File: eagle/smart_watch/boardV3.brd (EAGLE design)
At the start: 100 x 80 mm, 62 parts, among them U1 MCP73831, U2 TPS61200, U3 MAX1704X, U4 V_REG_LDOSMD, Y1 16MHz

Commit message: Did a little of bit of tweeks on the wireing
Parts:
- removed JP1: USB_MICROB_PLUG-PTH, SparkFun-Connectors:MICRO-B-RA-TH
- added RECHARGE: (no value), SparkFun-Connectors:MOLEX-1X2
- I2C: device SparkFun-Connectors:1X02_PP_HOLES_ONLY -> SparkFun-Connectors:MOLEX-1X2
- JP4: device SparkFun-Connectors:MOLEX-1X4 -> SparkFun-Connectors:1X05
- R12, R13: device SparkFun-Passives:0402-RES -> SparkFun-Resistors:0603-RES
- moved JP4 2.54 mm to (29.7, 1.35)
- moved R12 1.57 mm to (25.7, 15.1), turned to 90 degrees
- moved R18 0.54 mm to (39.2, 5.46)
- moved R13 0.51 mm to (22.4, 14.3)
- moved R17 0.40 mm to (43.1, 7.13)
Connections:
- net 3.3V: now also JP4.5
- net GND: now also RECHARGE.2; no longer JP1.5
- net VBUS: now also RECHARGE.1; no longer JP1.1
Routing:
- net 3.3V: track 108.8 -> 138.9 mm
- net JTAG_RESETX: track 18.7 -> 27.2 mm, vias 1 -> 2
- net SDA: track 45.9 -> 39.3 mm
- net GND: track 109.7 -> 105.5 mm
- net JTAG_TDO_SWOX: track 12.4 -> 15.6 mm, vias 0 -> 1
- net JTAG_TCLK_SWCLKX: track 9.00 -> 12.0 mm, vias 0 -> 1
- net MISO1: track 58.0 -> 60.2 mm, vias 3 -> 1
- net JTAG_TMS_SWDIOX: track 15.5 -> 13.7 mm
- net SSEL1: track 40.1 -> 38.6 mm
- net SCL: track 41.7 -> 40.9 mm
- net N$18: track 2.13 -> 2.67 mm
- net VBUS: track 6.75 -> 6.23 mm

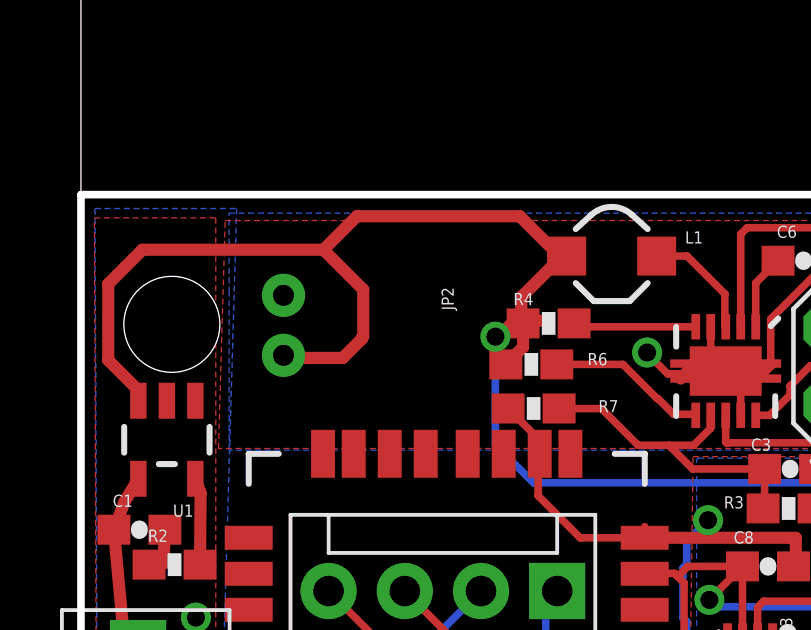
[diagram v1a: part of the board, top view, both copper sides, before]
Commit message: Fixed up git ignore for xpress;
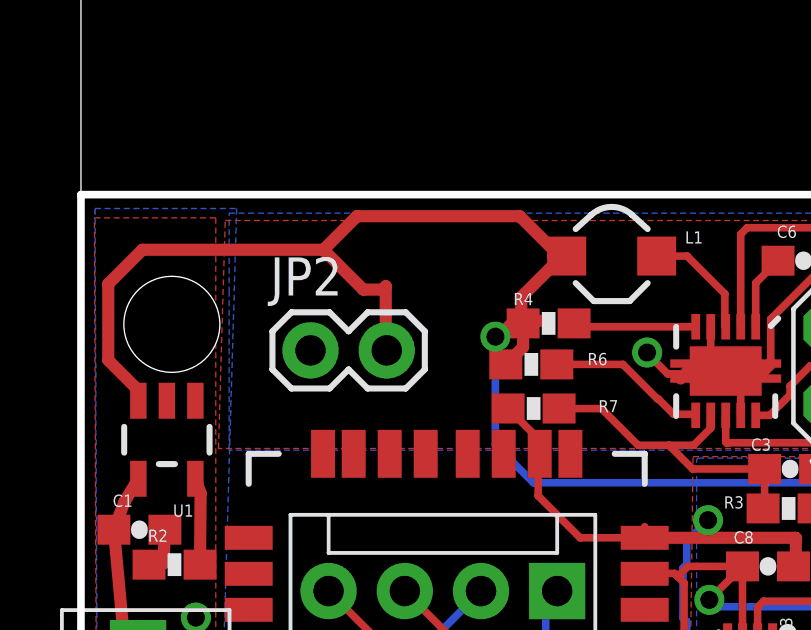
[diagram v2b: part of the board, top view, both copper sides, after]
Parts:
- JP2: device SparkFun-Connectors:JST-2-PTH-NS -> SparkFun-Connectors:1X02
- moved JP2 1.23 mm to (7.65, 30.9), turned to 0 degrees
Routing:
- net VBATT: track 74.0 -> 72.4 mm
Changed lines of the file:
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@@
 <attribute name="VALUE" x="3.81646875" y="28.093121875" size="0.4064" layer="27" rot="R180"/>
 </element>
-<element name="JP2" library="SparkFun-Connectors" package="JST-2-PTH-NS" value="" x="6.7517125" y="31.717434375" rot="R270"/>
+<element name="JP2" library="SparkFun-Connectors" package="1X02" value="" x="7.652565625" y="30.8817125"/>
 <element name="C1" library="SparkFun-Passives" package="0603-CAP" value="4.7uF" x="1.947775" y="24.904134375"/>
 <element name="R2" library="SparkFun-Passives" package="0603-RES" value="10k" x="3.119103125" y="23.739640625"/>
@@
 <wire x1="2.049053125" y1="34.2361125" x2="8.08201875" y2="34.2361125" width="0.4064" layer="1"/>
 <wire x1="8.08201875" y1="34.2361125" x2="9.41046875" y2="32.9076625" width="0.4064" layer="1"/>
-<wire x1="9.41046875" y1="32.9076625" x2="9.41046875" y2="31.3514625" width="0.4064" layer="1"/>
-<wire x1="9.41046875" y1="31.3514625" x2="9.372525" y2="31.31351875" width="0.4064" layer="1"/>
-<wire x1="9.372525" y1="31.31351875" x2="9.372525" y2="31.2753875" width="0.4064" layer="1"/>
-<wire x1="9.372525" y1="31.2753875" x2="8.727453125" y2="30.630315625" width="0.4064" layer="1"/>
-<wire x1="8.727453125" y1="30.630315625" x2="6.83883125" y2="30.630315625" width="0.4064" layer="1"/>
-<wire x1="6.83883125" y1="30.630315625" x2="6.7517125" y2="30.717434375" width="0.4064" layer="1"/>
 <wire x1="16.19140625" y1="34.0255" x2="15.754475" y2="34.0255" width="0.4064" layer="1"/>
 <wire x1="15.3046375" y1="31.872046875" x2="14.739209375" y2="31.781" width="0.4064" layer="1"/>
@@
 <wire x1="33.401" y1="22.098" x2="32.1843625" y2="22.098" width="0.254" layer="1"/>
 <wire x1="32.1843625" y1="22.098" x2="32.00883125" y2="21.92246875" width="0.254" layer="1"/>
+<wire x1="9.41046875" y1="32.9076625" x2="10.0476625" y2="32.9076625" width="0.4064" layer="1"/>
+<wire x1="10.0476625" y1="32.9076625" x2="10.16" y2="33.02" width="0.4064" layer="1"/>
+<wire x1="10.16" y1="33.02" x2="10.16" y2="30.914278125" width="0.4064" layer="1"/>
+<wire x1="10.16" y1="30.914278125" x2="10.192565625" y2="30.8817125" width="0.4064" layer="1"/>
 </signal>
 <signal name="N$3">

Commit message: Did a bunch of routing, woo... woo!!! woo?
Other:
- board size 100 x 80 mm -> 63.6 x 36.1 mm
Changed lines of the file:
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@@
 <grid distance="0.05" unitdist="inch" unit="inch" style="lines" multiple="10" display="yes" altdistance="0.005" altunitdist="inch" altunit="inch"/>
 <layers>
-<layer number="1" name="Top" color="4" fill="1" visible="yes" active="yes"/>
+<layer number="1" name="Top" color="4" fill="1" visible="no" active="yes"/>
 <layer number="2" name="Route2" color="1" fill="3" visible="no" active="yes"/>
 <layer number="3" name="Route3" color="4" fill="3" visible="no" active="yes"/>
@@
 <layer number="14" name="Route14" color="1" fill="6" visible="no" active="yes"/>
 <layer number="15" name="Route15" color="4" fill="6" visible="no" active="yes"/>
-<layer number="16" name="Bottom" color="1" fill="1" visible="yes" active="yes"/>
-<layer number="17" name="Pads" color="2" fill="1" visible="yes" active="yes"/>
-<layer number="18" name="Vias" color="2" fill="1" visible="yes" active="yes"/>
-<layer number="19" name="Unrouted" color="6" fill="1" visible="yes" active="yes"/>
+<layer number="16" name="Bottom" color="1" fill="1" visible="no" active="yes"/>
+<layer number="17" name="Pads" color="2" fill="1" visible="no" active="yes"/>
+<layer number="18" name="Vias" color="2" fill="1" visible="no" active="yes"/>
+<layer number="19" name="Unrouted" color="6" fill="1" visible="no" active="yes"/>
 <layer number="20" name="Dimension" color="15" fill="1" visible="yes" active="yes"/>
-<layer number="21" name="tPlace" color="16" fill="1" visible="yes" active="yes"/>
-<layer number="22" name="bPlace" color="14" fill="1" visible="yes" active="yes"/>
-<layer number="23" name="tOrigins" color="15" fill="1" visible="yes" active="yes"/>
-<layer number="24" name="bOrigins" color="15" fill="1" visible="yes" active="yes"/>
+<layer number="21" name="tPlace" color="16" fill="1" visible="no" active="yes"/>
+<layer number="22" name="bPlace" color="14" fill="1" visible="no" active="yes"/>
+<layer number="23" name="tOrigins" color="15" fill="1" visible="no" active="yes"/>
+<layer number="24" name="bOrigins" color="15" fill="1" visible="no" active="yes"/>
 <layer number="25" name="tNames" color="7" fill="1" visible="no" active="yes"/>
 <layer number="26" name="bNames" color="7" fill="1" visible="no" active="yes"/>
@@
 <layer number="29" name="tStop" color="7" fill="3" visible="no" active="yes"/>
 <layer number="30" name="bStop" color="7" fill="6" visible="no" active="yes"/>
-<layer number="31" name="tCream" color="7" fill="4" visible="no" active="yes"/>
+<layer number="31" name="tCream" color="7" fill="4" visible="yes" active="yes"/>
 <layer number="32" name="bCream" color="7" fill="5" visible="no" active="yes"/>
 <layer number="33" name="tFinish" color="6" fill="3" visible="no" active="yes"/>
@@
 <layer number="43" name="vRestrict" color="2" fill="10" visible="no" active="yes"/>
 <layer number="44" name="Drills" color="7" fill="1" visible="no" active="yes"/>
-<layer number="45" name="Holes" color="7" fill="1" visible="yes" active="yes"/>
+<layer number="45" name="Holes" color="7" fill="1" visible="no" active="yes"/>
 <layer number="46" name="Milling" color="3" fill="1" visible="no" active="yes"/>
 <layer number="47" name="Measures" color="7" fill="1" visible="no" active="yes"/>
@@
 <layer number="49" name="Reference" color="7" fill="1" visible="no" active="yes"/>
 <layer number="50" name="dxf" color="7" fill="1" visible="no" active="no"/>
-<layer number="51" name="tDocu" color="6" fill="1" visible="yes" active="yes"/>
+<layer number="51" name="tDocu" color="6" fill="1" visible="no" active="yes"/>
 <layer number="52" name="bDocu" color="7" fill="1" visible="no" active="yes"/>
 <layer number="53" name="tGND_GNDA" color="7" fill="9" visible="no" active="no"/>
@@
 <plain>
 <wire x1="63.467" y1="0" x2="63.5" y2="0" width="0" layer="20"/>
-<wire x1="63.5" y1="0" x2="100" y2="0" width="0" layer="20"/>
-<wire x1="100" y1="0" x2="100" y2="80" width="0" layer="20"/>
-<wire x1="100" y1="80" x2="0" y2="80" width="0" layer="20"/>
-<wire x1="0" y1="80" x2="0" y2="36.073615625" width="0" layer="20"/>
 <wire x1="0" y1="0" x2="0" y2="36.073615625" width="0.254" layer="20"/>
 <wire x1="0" y1="0" x2="63.467" y2="0" width="0.254" layer="20"/>
